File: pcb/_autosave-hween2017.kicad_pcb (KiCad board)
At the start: 2 copper layers, 86.4 x 66 mm, 36 parts, among them J1 BATTERY, J2 JTAG, K1 SY-3W-K, K2 SY-3W-K, U1 HV509, U2 MSP430FR2100IPW

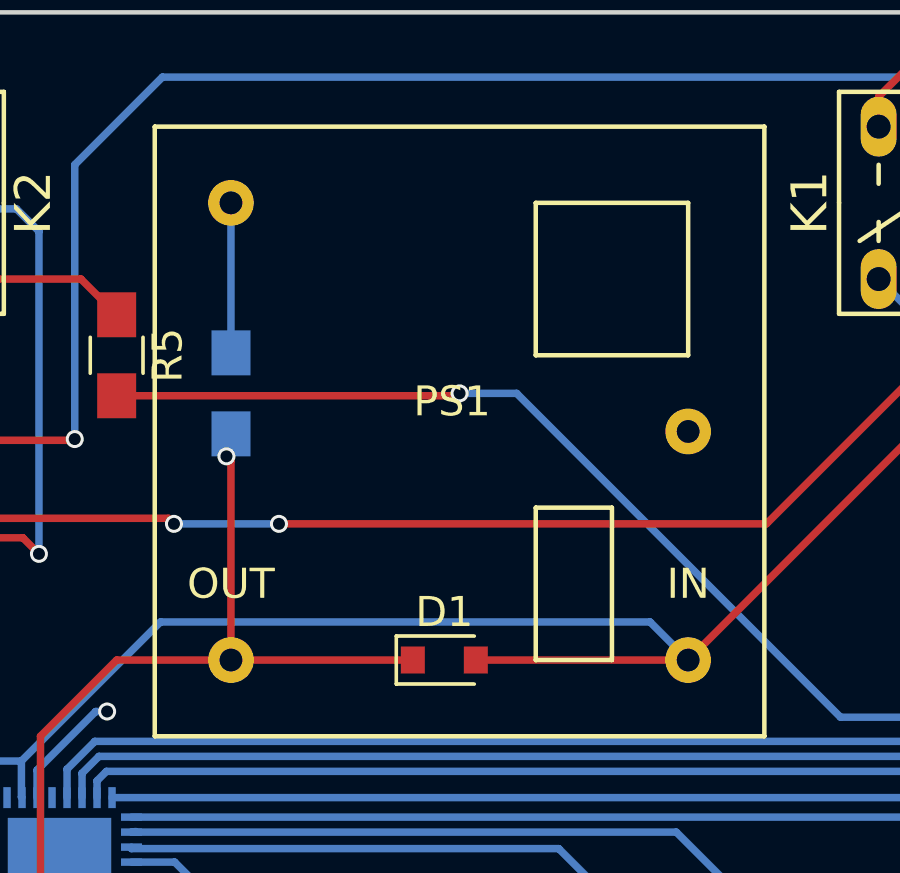
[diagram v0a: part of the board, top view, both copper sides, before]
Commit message: Add new PCB changes and a stencil STL file.
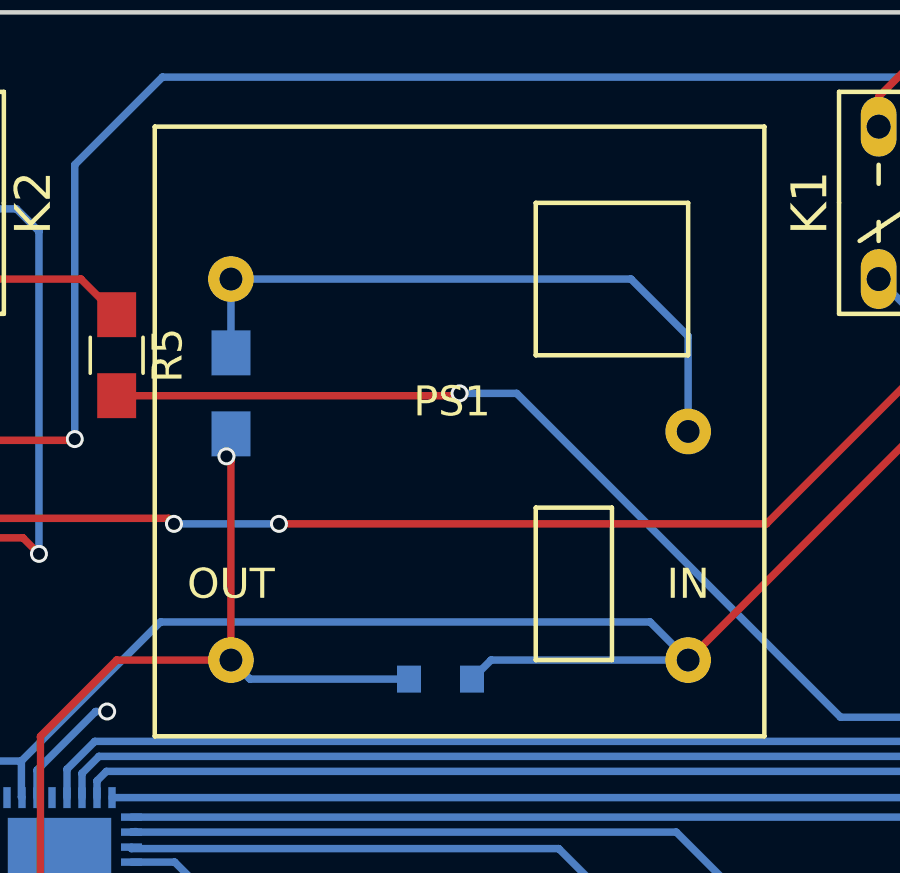
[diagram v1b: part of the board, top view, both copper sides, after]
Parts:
- D1: moved to B.Cu
- moved D1 0.65 mm to (83.2, 84.5)
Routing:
- net Earth: track 38.2 -> 54.9 mm
